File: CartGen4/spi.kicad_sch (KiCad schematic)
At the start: 11 parts, among them J1 MEM2080-00-128-00-A, U1 DS1391U-33+, U2 IS25WP080D-JNLE, Y1 FC-135R 32.7680KA-E5

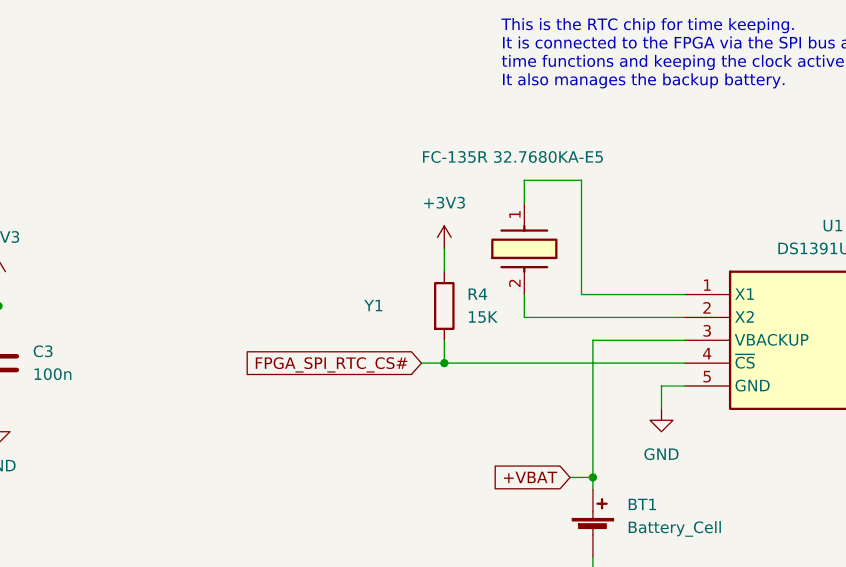
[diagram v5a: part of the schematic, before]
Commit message: Fixed silk screen placement Fixed RD misplacement Changed R16 supplier suggestion
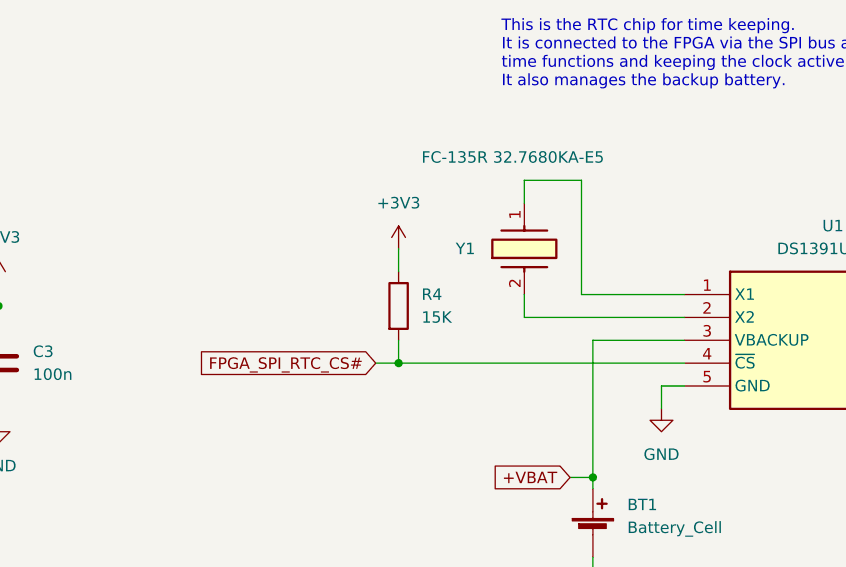
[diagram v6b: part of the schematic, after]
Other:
- moved on the sheet: R4
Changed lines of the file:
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@@
   (junction (at 58.42 135.89) (diameter 0) (color 0 0 0 0)
   )
-  (junction (at 167.64 76.2) (diameter 0) (color 0 0 0 0)
+  (junction (at 162.56 76.2) (diameter 0) (color 0 0 0 0)
   )
   (junction (at 66.04 125.73) (diameter 0) (color 0 0 0 0)
@@
     (stroke (width 0) (type default) (color 0 0 0 0))
   )
-  (wire (pts (xy 167.64 73.66) (xy 167.64 76.2))
+  (wire (pts (xy 162.56 73.66) (xy 162.56 76.2))
     (stroke (width 0) (type default) (color 0 0 0 0))
   )
@@
     (stroke (width 0) (type default) (color 0 0 0 0))
   )
-  (wire (pts (xy 165.1 76.2) (xy 167.64 76.2))
-    (stroke (width 0) (type default) (color 0 0 0 0))
-  )
-  (wire (pts (xy 167.64 76.2) (xy 194.31 76.2))
+  (wire (pts (xy 160.02 76.2) (xy 162.56 76.2))
+    (stroke (width 0) (type default) (color 0 0 0 0))
+  )
+  (wire (pts (xy 162.56 76.2) (xy 194.31 76.2))
     (stroke (width 0) (type default) (color 0 0 0 0))
   )
@@
     (stroke (width 0) (type default) (color 0 0 0 0))
   )
-  (wire (pts (xy 167.64 63.5) (xy 167.64 66.04))
+  (wire (pts (xy 162.56 63.5) (xy 162.56 66.04))
     (stroke (width 0) (type default) (color 0 0 0 0))
   )
@@
     )
   )
-  (global_label "FPGA_SPI_RTC_CS#" (shape input) (at 165.1 76.2 180) (fields_autoplaced)
+  (global_label "FPGA_SPI_RTC_CS#" (shape input) (at 160.02 76.2 180) (fields_autoplaced)
     (effects (font (size 1.27 1.27)) (justify right))
-    (property "Intersheet References" "${INTERSHEET_REFS}" (id 0) (at 144.7255 76.1206 0)
+    (property "Intersheet References" "${INTERSHEET_REFS}" (id 0) (at 139.6455 76.1206 0)
       (effects (font (size 1.27 1.27)) (justify right) hide)
     )
@@
     (pin "1")
   )
-  (symbol (lib_id "Device:R") (at 167.64 69.85 0) (unit 1)
-    (in_bom yes) (on_board yes) (fields_autoplaced)
-    (property "Reference" "R4" (id 0) (at 170.18 68.5799 0)
-      (effects (font (size 1.27 1.27)) (justify left))
-    )
-    (property "Value" "15K" (id 1) (at 170.18 71.1199 0)
-      (effects (font (size 1.27 1.27)) (justify left))
-    )
-    (property "Footprint" "Resistor_SMD:R_0402_1005Metric_Pad0.72x0.64mm_HandSolder" (id 2) (at 165.862 69.85 90)
-      (effects (font (size 1.27 1.27)) hide)
-    )
-    (property "Datasheet" "~" (id 3) (at 167.64 69.85 0)
-      (effects (font (size 1.27 1.27)) hide)
-    )
-    (property "Tolerance" "10%" (id 4) (at 167.64 69.85 0)
-      (effects (font (size 1.27 1.27)) hide)
-    )
-    (property "Source" "ANY" (id 5) (at 167.64 69.85 0)
-      (effects (font (size 1.27 1.27)) hide)
-    )
-    (property "Critical" "Y" (id 6) (at 167.64 69.85 0)
-      (effects (font (size 1.27 1.27)) hide)
-    )
-    (property "Notes" "Pullup resistor for ensuring that slave is not selecting during startup" (id 7) (at 167.64 69.85 0)
-      (effects (font (size 1.27 1.27)) hide)
-    )
-    (property "Description" "~" (id 8) (at 167.64 69.85 0)
-      (effects (font (size 1.27 1.27)) hide)
-    )
-    (property "MFN" "~" (id 9) (at 167.64 69.85 0)
-      (effects (font (size 1.27 1.27)) hide)
-    )
-    (property "MFP" "~" (id 10) (at 167.64 69.85 0)
-      (effects (font (size 1.27 1.27)) hide)
-    )
-    (property "Package ID" "0402" (id 11) (at 167.64 69.85 0)
-      (effects (font (size 1.27 1.27)) hide)
-    )
-    (property "Supplier suggestion" "https://nl.mouser.com/ProductDetail/Kamaya/RMC1-16S-153JTH?qs=sGAEpiMZZMvdGkrng054t%252BjmMOhbS7JJ11bN0iqZRdOn%2Fu9rqH1%2FEw%3D%3D" (id 12) (at 167.64 69.85 0)
+  (symbol (lib_id "Device:R") (at 162.56 69.85 0) (unit 1)
+    (in_bom yes) (on_board yes) (fields_autoplaced)
+    (property "Reference" "R4" (id 0) (at 165.1 68.5799 0)
+      (effects (font (size 1.27 1.27)) (justify left))
+    )
+    (property "Value" "15K" (id 1) (at 165.1 71.1199 0)
+      (effects (font (size 1.27 1.27)) (justify left))
+    )
+    (property "Footprint" "Resistor_SMD:R_0402_1005Metric_Pad0.72x0.64mm_HandSolder" (id 2) (at 160.782 69.85 90)
+      (effects (font (size 1.27 1.27)) hide)
+    )
+    (property "Datasheet" "~" (id 3) (at 162.56 69.85 0)
+      (effects (font (size 1.27 1.27)) hide)
+    )
+    (property "Tolerance" "10%" (id 4) (at 162.56 69.85 0)
+      (effects (font (size 1.27 1.27)) hide)
+    )
+    (property "Source" "ANY" (id 5) (at 162.56 69.85 0)
+      (effects (font (size 1.27 1.27)) hide)
+    )
+    (property "Critical" "Y" (id 6) (at 162.56 69.85 0)
+      (effects (font (size 1.27 1.27)) hide)
+    )
+    (property "Notes" "Pullup resistor for ensuring that slave is not selecting during startup" (id 7) (at 162.56 69.85 0)
+      (effects (font (size 1.27 1.27)) hide)
+    )
+    (property "Description" "~" (id 8) (at 162.56 69.85 0)
+      (effects (font (size 1.27 1.27)) hide)
+    )
+    (property "MFN" "~" (id 9) (at 162.56 69.85 0)
+      (effects (font (size 1.27 1.27)) hide)
+    )
+    (property "MFP" "~" (id 10) (at 162.56 69.85 0)
+      (effects (font (size 1.27 1.27)) hide)
+    )
+    (property "Package ID" "0402" (id 11) (at 162.56 69.85 0)
+      (effects (font (size 1.27 1.27)) hide)
+    )
+    (property "Supplier suggestion" "https://nl.mouser.com/ProductDetail/Kamaya/RMC1-16S-153JTH?qs=sGAEpiMZZMvdGkrng054t%252BjmMOhbS7JJ11bN0iqZRdOn%2Fu9rqH1%2FEw%3D%3D" (id 12) (at 162.56 69.85 0)
       (effects (font (size 1.27 1.27)) hide)
     )
@@
   (symbol (lib_id "SamacSys_Parts:FC-135R_32.7680KA-E5") (at 176.53 68.58 90) (unit 1)
     (in_bom yes) (on_board yes)
-    (property "Reference" "Y1" (id 0) (at 158.75 69.85 90)
+    (property "Reference" "Y1" (id 0) (at 168.91 63.5 90)
       (effects (font (size 1.27 1.27)) (justify right))
     )
@@
     (pin "1")
   )
-  (symbol (lib_id "power:+3V3") (at 167.64 63.5 0) (unit 1)
-    (in_bom yes) (on_board yes) (fields_autoplaced)
-    (property "Reference" "#PWR081" (id 0) (at 167.64 67.31 0)
-      (effects (font (size 1.27 1.27)) hide)
-    )
-    (property "Value" "+3V3" (id 1) (at 167.64 58.42 0))
-    (property "Footprint" "" (id 2) (at 167.64 63.5 0)
-      (effects (font (size 1.27 1.27)) hide)
-    )
-    (property "Datasheet" "" (id 3) (at 167.64 63.5 0)
-      (effects (font (size 1.27 1.27)) hide)
-    )
+  (symbol (lib_id "power:+3V3") (at 162.56 63.5 0) (unit 1)
+    (in_bom yes) (on_board yes) (fields_autoplaced)
+    (property "Reference" "#PWR081" (id 0) (at 162.56 67.31 0)
+      (effects (font (size 1.27 1.27)) hide)
+    )
+    (property "Value" "+3V3" (id 1) (at 162.56 58.42 0))
+    (property "Footprint" "" (id 2) (at 162.56 63.5 0)
+      (effects (font (size 1.27 1.27)) hide)
+    )
+    (property "Datasheet" "" (id 3) (at 162.56 63.5 0)
+      (effects (font (size 1.27 1.27)) hide)
+    )
